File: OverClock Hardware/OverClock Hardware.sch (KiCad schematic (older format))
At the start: 0 parts

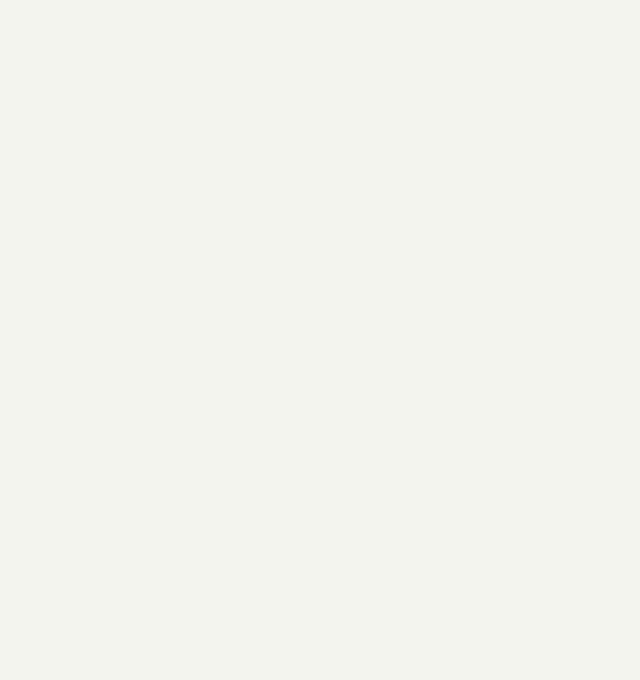
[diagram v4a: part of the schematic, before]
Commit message: Interfaced Hours Digits to FPGA
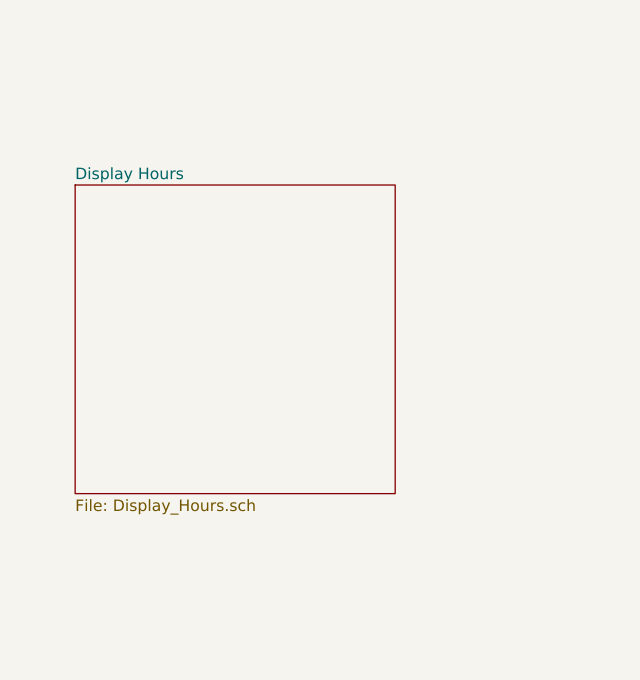
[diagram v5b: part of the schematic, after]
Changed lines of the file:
@@
 $Descr A4 11693 8268
 encoding utf-8
-Sheet 1 3
+Sheet 1 4
 Title ""
 Date ""
@@
 F1 "FPGA_Interfacing.sch" 50
 $EndSheet
+$Sheet
+S 1650 4350 1400 1350
+U 5C87E0ED
+F0 "Display Hours" 50
+F1 "Display_Hours.sch" 50
+$EndSheet
 $EndSCHEMATC

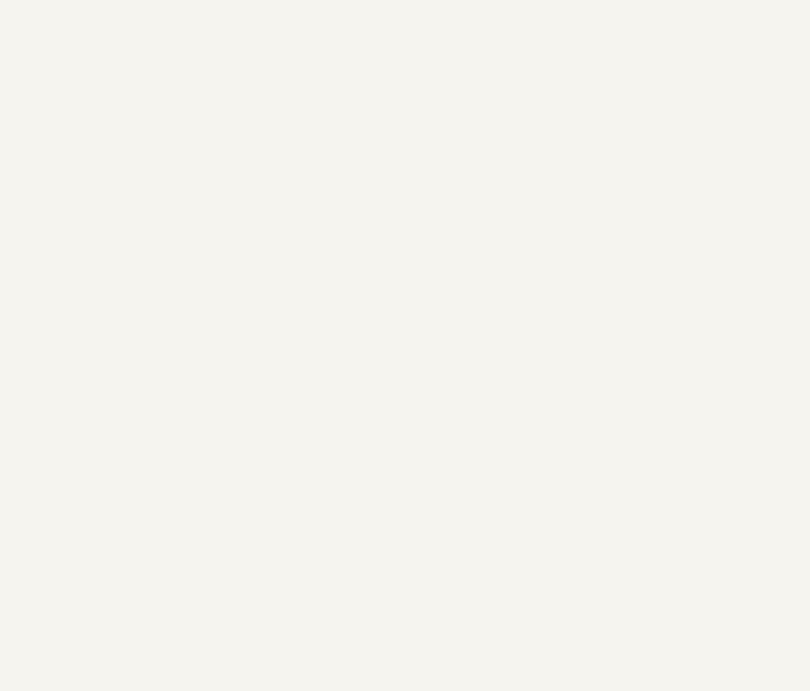
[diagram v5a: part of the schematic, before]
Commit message: Interfaced minutes digits to FPGA and added time selection methods
Interfaced the two 7 Segment displays used for displaying the minutes to the FPGA. 

Added 4 Tactile switches to increment/decrement the hours and minutes separately.

Added a header to allow for setting of the time via UART.
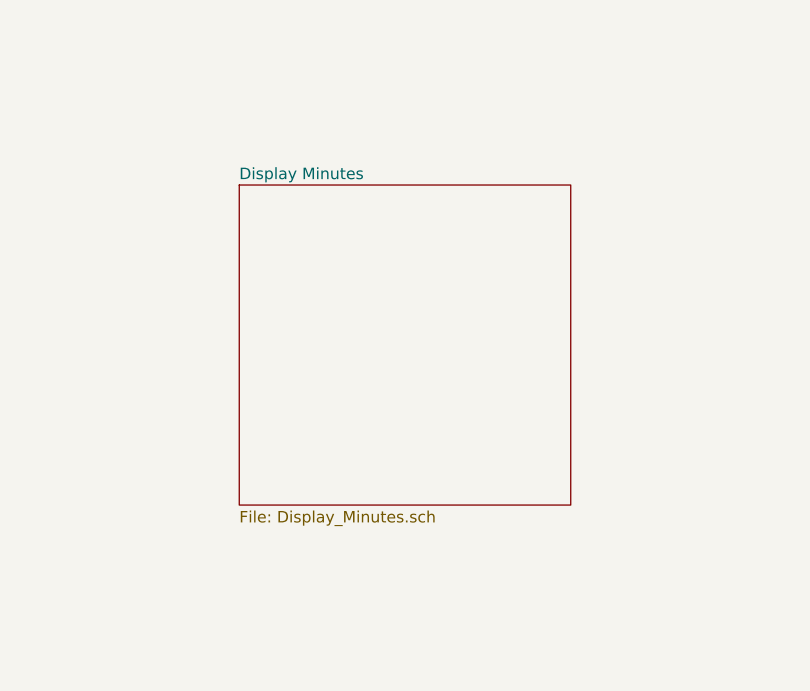
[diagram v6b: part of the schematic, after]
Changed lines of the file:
@@
 $Descr A4 11693 8268
 encoding utf-8
-Sheet 1 4
+Sheet 1 5
 Title ""
 Date ""
@@
 F1 "Display_Hours.sch" 50
 $EndSheet
+$Sheet
+S 4650 4350 1450 1400
+U 5C9EFB73
+F0 "Display Minutes" 50
+F1 "Display_Minutes.sch" 50
+$EndSheet
 $EndSCHEMATC

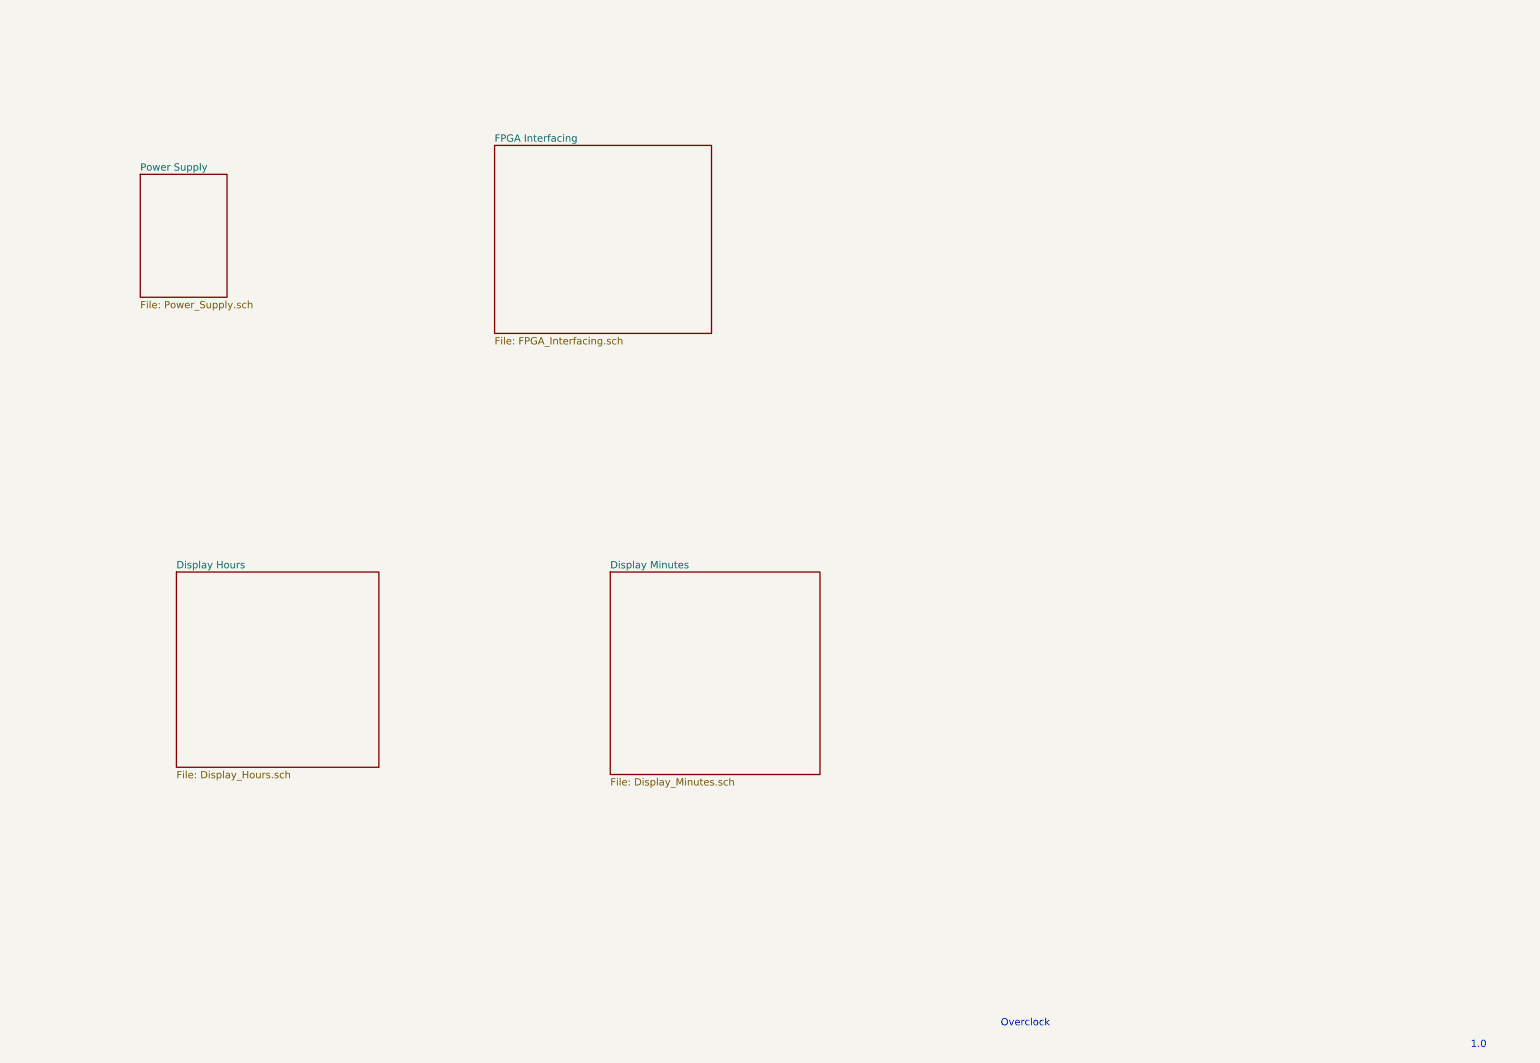
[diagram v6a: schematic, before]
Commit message: Added Functional Block DIagram to Schematic
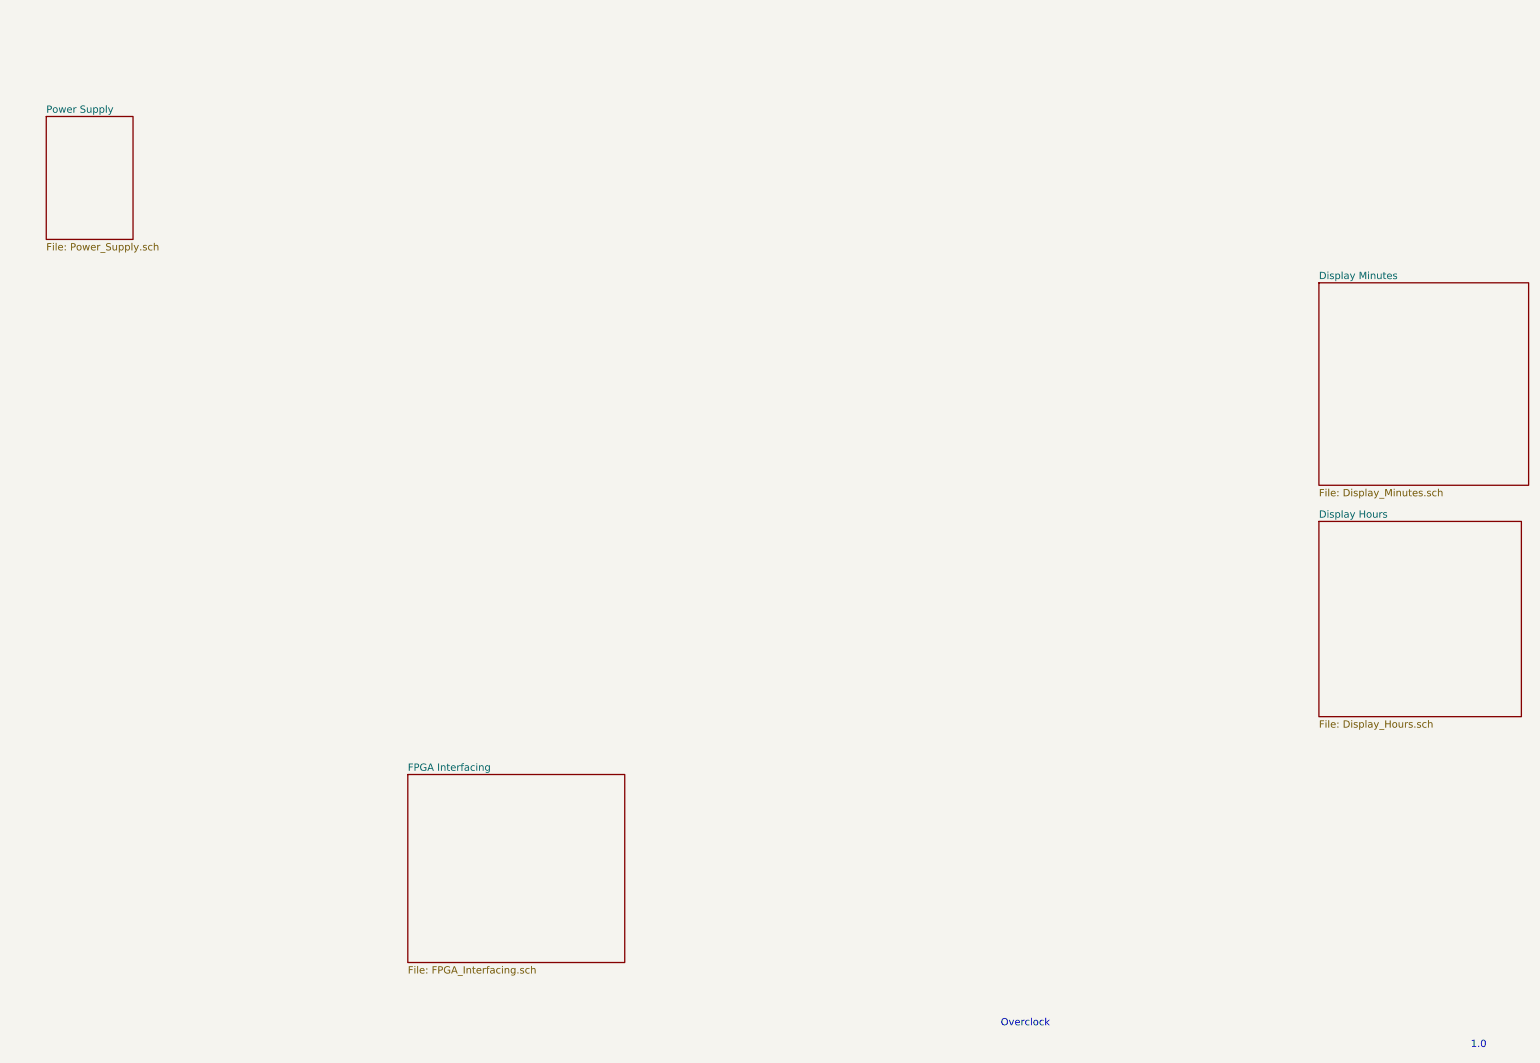
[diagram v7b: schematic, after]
